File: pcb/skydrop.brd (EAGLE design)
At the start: 104.2 x 83 mm, 101 parts, among them IC1 RT9193-33GB, IC2 MCP73831/OT, IC3 STM809SWX6F, IC4 MS5611-01BA03, Q1 BSS84, Q10 BSS84, Q2 BSS123, Q3 BSS123, Q5 BSS84, Q6 BSS84, Q7 BSS123, Q8 BSS84, Q9 BSS84, U2 W25Q16BVSS

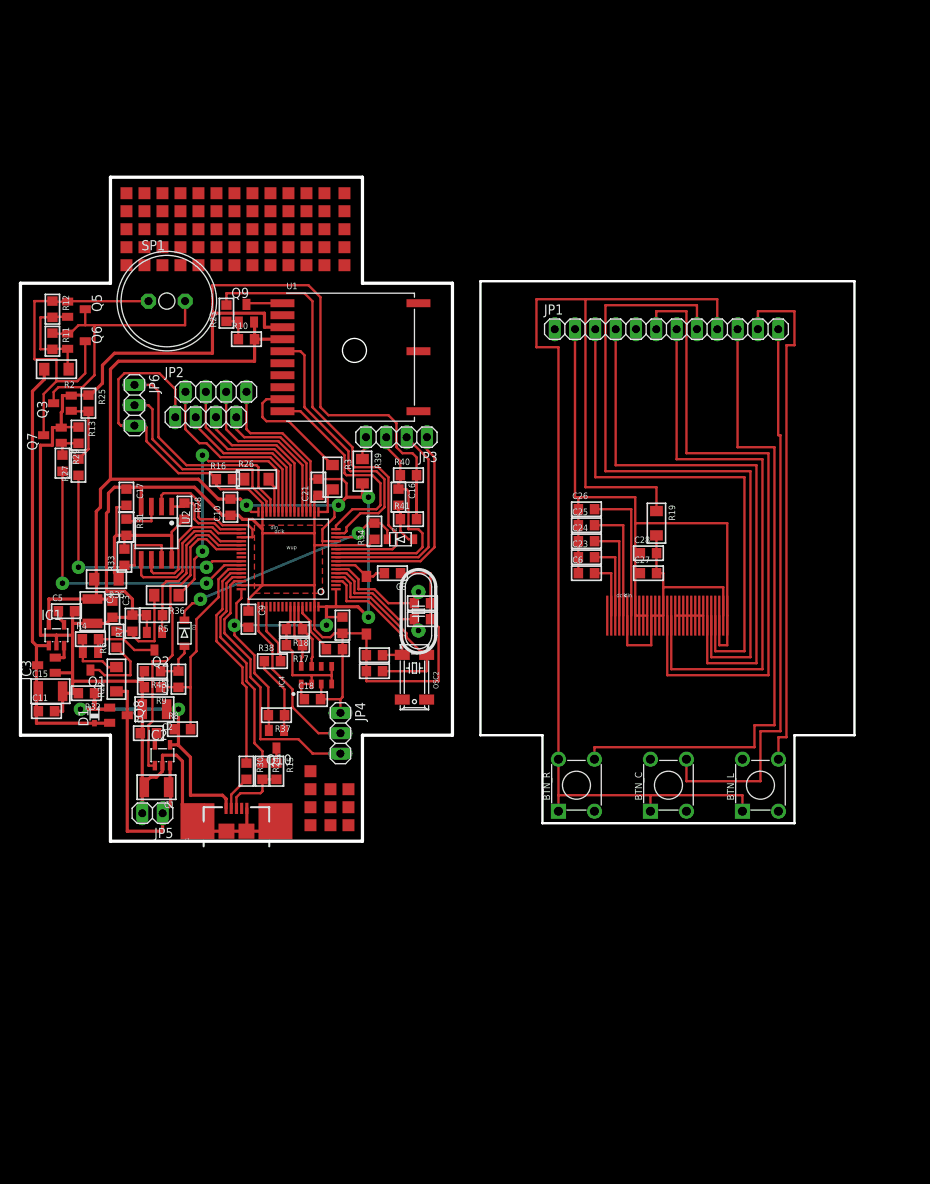
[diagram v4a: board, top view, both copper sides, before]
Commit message: improve pcb for new display
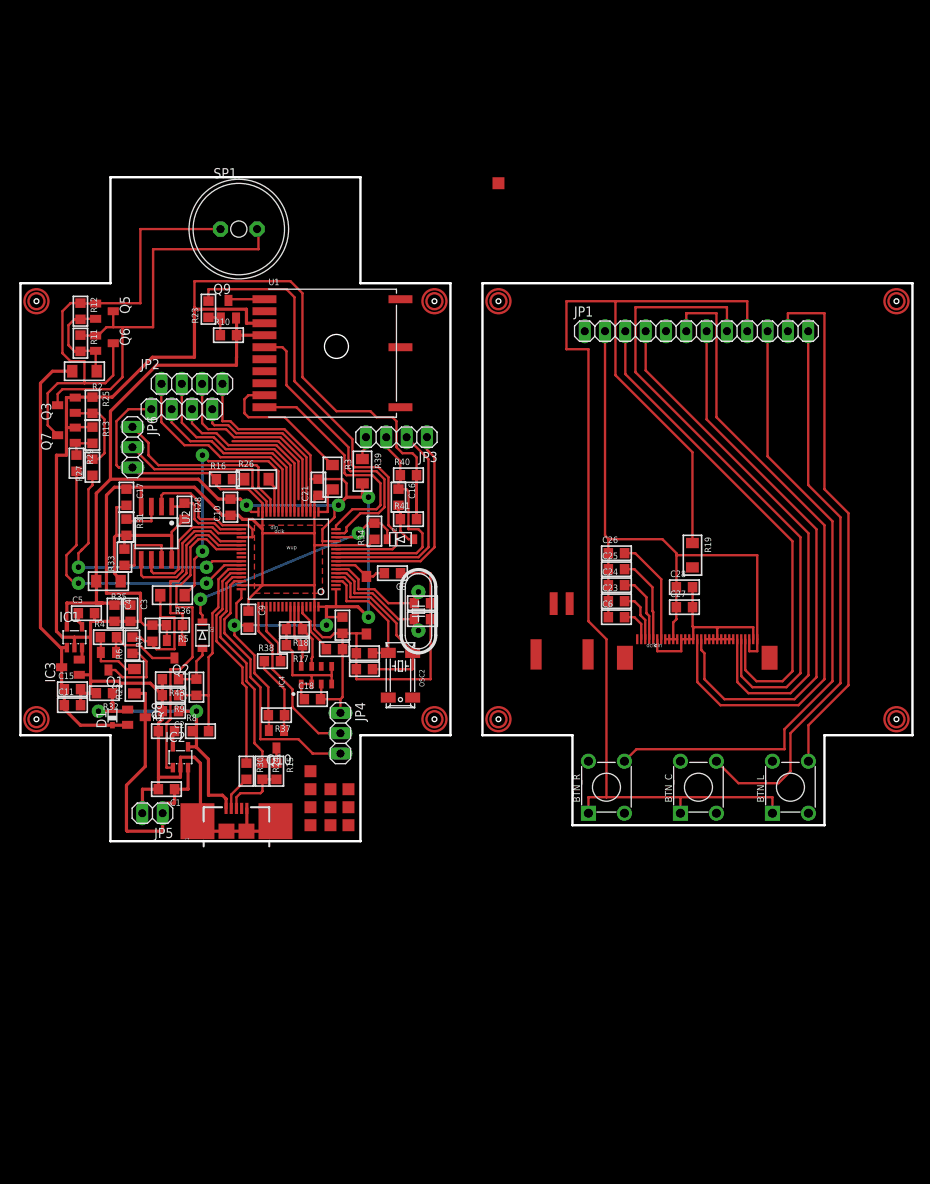
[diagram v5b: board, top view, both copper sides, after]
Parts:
- C1, C15, C2, C4: device skydrop:C1210 -> skydrop:C0805
- moved SP1 12.7 mm to (29.8, 77.0)
- moved C23 6.66 mm to (77.0, 30.5)
- moved C24 6.66 mm to (77.0, 32.5)
- moved C25 6.66 mm to (77.0, 34.5)
- moved C26 6.66 mm to (77.0, 36.5)
- moved C6 6.66 mm to (77.0, 28.5)
- moved C27 6.19 mm to (85.5, 29.8)
- moved C28 6.19 mm to (85.5, 32.2)
- moved R19 6.02 mm to (86.5, 36.2)
- moved JP6 5.26 mm to (16.5, 49.8)
- moved BTN_C 3.76 mm to (87.2, 7.25)
- moved BTN_L 3.76 mm to (98.8, 7.25)
- moved BTN_R 3.76 mm to (75.8, 7.25)
- moved JP1 3.76 mm to (87.0, 64.2)
- moved U$1 3.76 mm to (111.2, 12.8)
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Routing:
- net N$41: track 35.7 -> 53.8 mm
- net N$42: track 42.4 -> 59.5 mm
- net N$26: track 0.00 -> 14.0 mm
- net GND: track 418.1 -> 405.7 mm
- net N$15: track 37.3 -> 28.3 mm
- net LCD_CE_T: track 67.0 -> 62.0 mm
- net LCD_RST_T: track 86.7 -> 82.0 mm
- net N$50: track 17.9 -> 13.4 mm
- net N$33: track 29.3 -> 25.0 mm
- net LCD_DC_T: track 71.5 -> 67.2 mm
- net N$34: track 26.3 -> 22.2 mm
- net LCD_CLK_B: track 21.9 -> 25.9 mm
- net LCD_RST_B: track 18.1 -> 22.1 mm
- net N$49: track 14.9 -> 11.0 mm
- net LCD_DC_B: track 20.1 -> 23.9 mm
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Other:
- board size 104.2 x 83 mm -> 111.5 x 83 mm

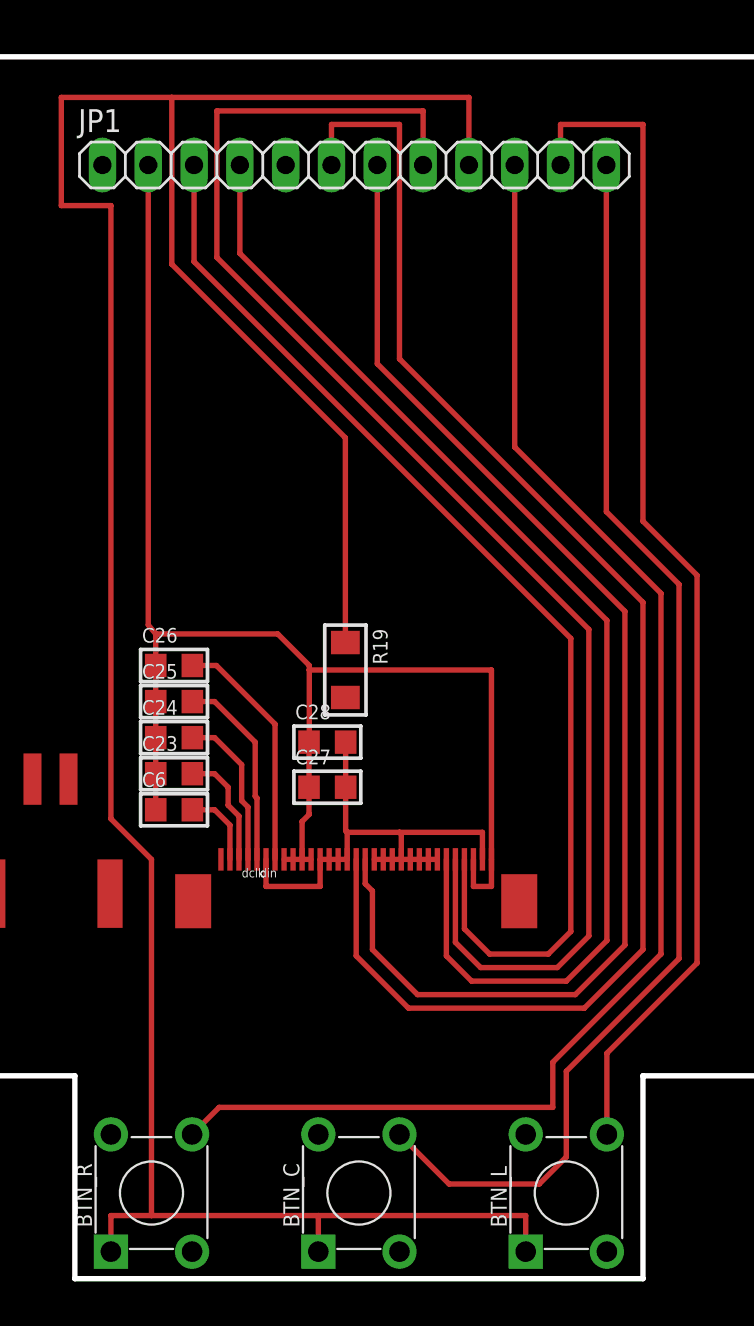
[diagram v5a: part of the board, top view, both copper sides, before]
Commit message: add spi extender
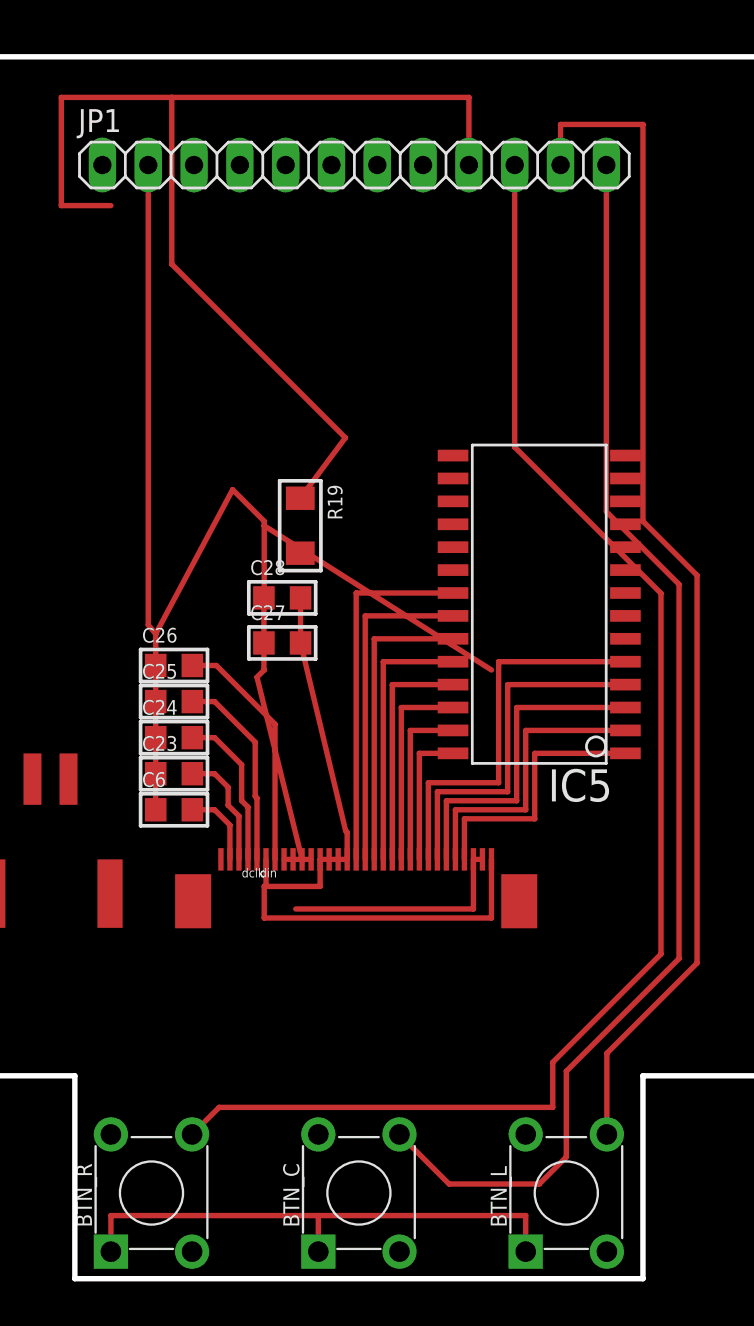
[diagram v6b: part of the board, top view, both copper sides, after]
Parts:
- added IC5: MCP23S17SO, skydrop:SO28W
- moved C27 8.38 mm to (83.0, 37.8)
- moved C28 8.38 mm to (83.0, 40.2)
- moved R19 8.38 mm to (84.0, 44.2)
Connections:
- new net N$51: IC5.28, U$1.9
- new net N$53: IC5.27, U$1.10
- new net N$54: IC5.26, U$1.11
- new net N$55: IC5.25, U$1.12
- new net N$56: IC5.24, U$1.13
- new net N$57: IC5.23, U$1.14
- new net N$58: IC5.22, U$1.15
- new net N$59: IC5.21, U$1.16
- new net N$60: IC5.1, U$1.4
- new net N$61: IC5.2, U$1.5
- new net N$62: IC5.3, U$1.6
- new net N$63: IC5.4, U$1.7
- new net N$64: IC5.5, U$1.8
- new net VDD: IC5.9
- new net VSS: IC5.10
- net GND_T: now also U$1.2; no longer U$1.1
- net LCD_CE_T: no longer U$1.4
- net LCD_CLK_T: no longer U$1.15
- net LCD_DC_T: no longer U$1.6
- net LCD_DIN_T: no longer U$1.16
- net LCD_RST_T: no longer U$1.5
- net N$15: now also U$1.1; no longer U$1.10, U$1.11, U$1.12, U$1.13, U$1.14, U$1.2, U$1.7, U$1.8, U$1.9
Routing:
- net LCD_RST_T: track 82.0 -> 0.00 mm
- net LCD_DIN_T: track 81.2 -> 0.00 mm
- net LCD_CLK_T: track 70.3 -> 0.00 mm
- net LCD_DC_T: track 67.2 -> 0.00 mm
- net VCC_T: track 155.2 -> 91.1 mm
- net LCD_CE_T: track 62.0 -> 0.00 mm
- net N$64: track 0.00 -> 21.9 mm
- net N$59: track 0.00 -> 20.1 mm
- net N$63: track 0.00 -> 20.1 mm
- net N$58: track 0.00 -> 18.4 mm
- net N$62: track 0.00 -> 18.4 mm
- net N$57: track 0.00 -> 16.6 mm
- net N$61: track 0.00 -> 16.6 mm
- net N$56: track 0.00 -> 14.8 mm
- net N$60: track 0.00 -> 14.8 mm
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
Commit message: improove spi extender
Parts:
- added R20: 0, skydrop:R1206
- moved R19 4.26 mm to (79.8, 44.0)
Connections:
- removed net LCD_DC_B: JP2.3, UC1.P$25
- removed net LCD_DC_T: JP1.4
- removed net LCD_PWR_B: JP2.4, UC1.P$24
- removed net LCD_PWR_T: JP1.5
- removed net VDD: IC5.9
- removed net VSS: IC5.10
- new net LCD_DOUT_B: JP2.6, UC1.P$22
- new net LCD_DOUT_T: IC5.14, JP1.7
- new net N$65: R20.2, U$1.2, U$1.3
- net GND_T: now also IC5.10, IC5.15, IC5.16, IC5.17; no longer U$1.2, U$1.3
- net LCD_CE_B: now also JP2.4, UC1.P$24; no longer JP2.2, UC1.P$26
- net LCD_CE_T: now also IC5.11, JP1.5; no longer JP1.3
- net LCD_CLK_B: now also JP2.7; no longer JP2.6
- net LCD_CLK_T: now also IC5.12, JP1.8; no longer JP1.7
- net LCD_DIN_T: now also IC5.13
- net LCD_RST_B: now also JP2.3, UC1.P$25; no longer JP2.7, UC1.P$20
- net LCD_RST_T: now also IC5.18, JP1.4; no longer JP1.8
- net VCC_T: now also IC5.9
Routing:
- net GND_T: track 96.2 -> 135.6 mm
- net LCD_CE_T: track 0.00 -> 38.8 mm
- net LCD_DIN_T: track 0.00 -> 33.7 mm
- net LCD_CLK_T: track 0.00 -> 32.8 mm
- net LCD_RST_T: track 0.00 -> 31.7 mm
- net LCD_DOUT_T: track 0.00 -> 29.9 mm
- net LCD_PWR_B: track 26.5 -> 0.00 mm
- net LCD_DOUT_B: track 0.00 -> 25.4 mm
- net LCD_DC_B: track 23.9 -> 0.00 mm
- net N$26: track 14.0 -> 0.00 mm
- net N$65: track 0.00 -> 13.1 mm
- net BTN_L_T: track 66.1 -> 75.3 mm
- net BTN_C_T: track 70.3 -> 78.3 mm
- net BTN_R_T: track 78.7 -> 86.1 mm
- net LCD_CLK_B: track 25.9 -> 21.5 mm
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
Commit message: [pcb] improove
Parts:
- added Q4: BSS123, transistor-small-signal:SOT23
- added R21: 100k, skydrop:R0805
- added R42: 10k, skydrop:R0805
- moved R20 100.9 mm to (100.2, 25.8), turned to 90 degrees
- moved C26 10.5 mm to (83.8, 28.5), turned to 180 degrees
- moved C6 10.5 mm to (83.8, 36.5), turned to 180 degrees
- moved C23 7.85 mm to (83.8, 34.5), turned to 180 degrees
- moved C25 7.85 mm to (83.8, 30.5), turned to 180 degrees
- moved C24 6.75 mm to (83.8, 32.5), turned to 180 degrees
- moved R19 3.76 mm to (83.5, 43.8), turned to 0 degrees
- moved C27 1.80 mm to (84.5, 38.8)
- moved C28 1.58 mm to (84.5, 40.8)
- moved JP1 0.50 mm to (87.5, 64.2), flipped to the bottom
- turned BTN_L to 270 degrees
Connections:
- removed net N$25: BTN_L.2
- removed net N$36: BTN_C.2
- removed net N$52: BTN_R.2
- new net LCD_PWM_B: JP2.3, UC1.P$26
- new net LCD_PWM_T: JP1.4, Q4.1, R42.1
- new net N$26: Q4.3, U$1.K
- net BTN_C_T: now also BTN_C.2, JP1.10; no longer JP1.12
- net BTN_L_T: now also BTN_L.2
- net BTN_R_T: now also BTN_R.2, JP1.12; no longer JP1.10
- net GND_T: now also Q4.2, R20.1, R21.2, R42.2
- net LCD_CE_B: now also JP2.8, UC1.P$20; no longer JP2.4, UC1.P$24
- net LCD_CE_T: now also JP1.9; no longer JP1.5
- net LCD_RST_B: now also JP2.4, UC1.P$24; no longer JP2.3, UC1.P$25
- net LCD_RST_T: now also JP1.5, R19.1; no longer IC5.18, JP1.4
- net N$15: now also IC5.18, R21.1; no longer C27.2, C28.2, U$1.1, U$1.17, U$1.18, U$1.19, U$1.20, U$1.26
- net VCC: now also JP2.2; no longer JP2.8
- net VCC_T: now also C27.2, C28.2, JP1.3, U$1.1, U$1.17, U$1.18, U$1.19, U$1.20, U$1.26, U$1.A; no longer JP1.9, R19.1
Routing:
- net VCC_T: track 87.1 -> 206.9 mm
- net LCD_PWM_T: track 0.00 -> 51.5 mm
- net N$15: track 40.2 -> 7.81 mm
- net LCD_PWM_B: track 0.00 -> 23.6 mm
- net BTN_R_T: track 86.1 -> 63.3 mm
- net VCC: track 203.2 -> 185.2 mm
- net BTN_L_T: track 75.3 -> 92.8 mm
- net N$50: track 13.4 -> 2.75 mm
- net BTN_C_T: track 78.3 -> 67.7 mm
- net LCD_CE_T: track 38.8 -> 49.0 mm
- net N$40: track 4.34 -> 13.4 mm
- net N$26: track 0.00 -> 5.49 mm
- net N$49: track 11.0 -> 5.88 mm
- net LCD_DIN_T: track 33.7 -> 28.7 mm
- net N$65: track 13.1 -> 8.15 mm
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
